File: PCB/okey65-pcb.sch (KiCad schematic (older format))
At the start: 14 parts

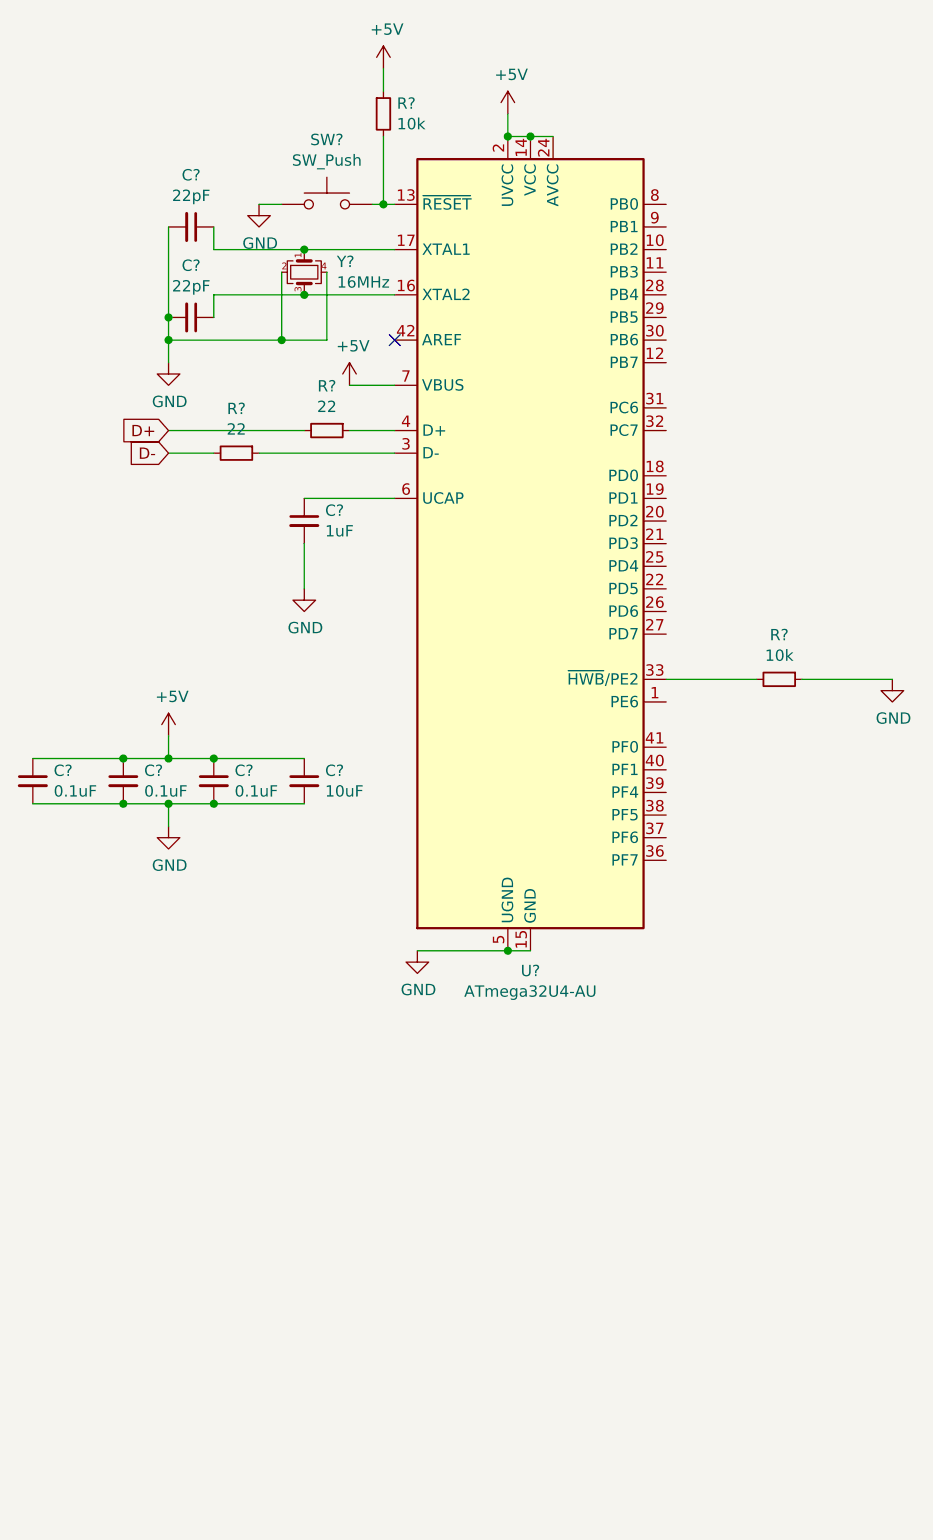
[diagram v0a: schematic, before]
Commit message: USB circuit shematic
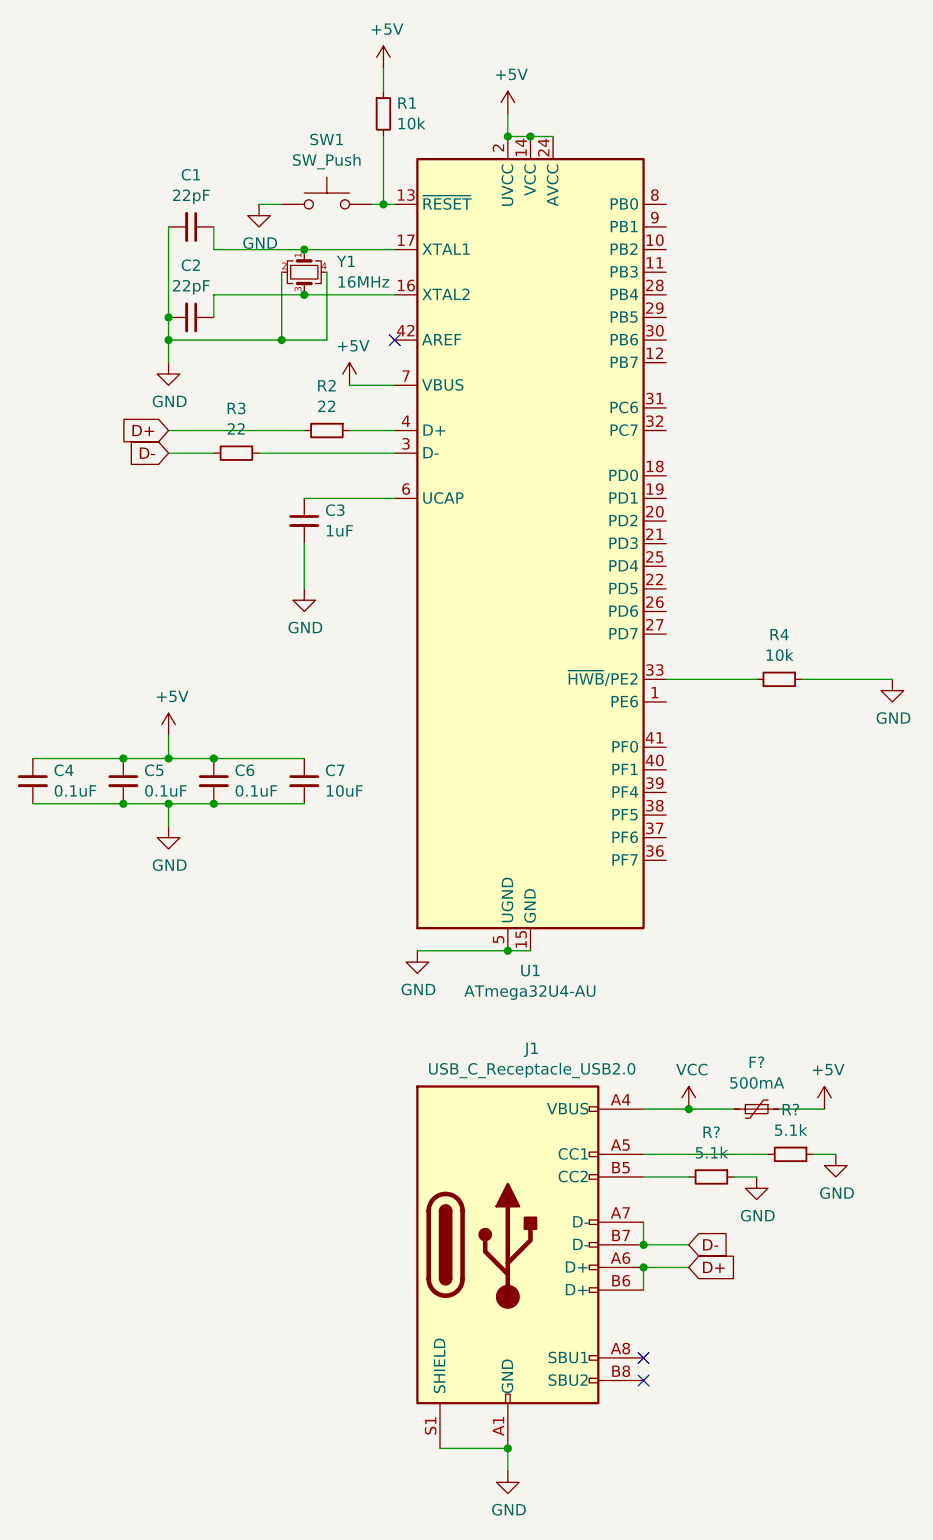
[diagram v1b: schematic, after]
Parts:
- added F?: 500mA, symbol Device:Polyfuse_Small
- added J1: USB_C_Receptacle_USB2.0, Connector_USB:USB_C_Receptacle_Palconn_UTC16-G, symbol Connector:USB_C_Receptacle_USB2.0
- added R? (x2): 5.1k, symbol Device:R_Small
- C1, C2, C3, C4, C5, C6, C7: renamed from C?; footprint (none) -> Capacitor_SMD:C_0805_2012Metric
- R1, R2, R3, R4: renamed from R?; footprint (none) -> Resistor_SMD:R_0805_2012Metric
- SW1: renamed from SW?; footprint (none) -> random-keyboard-parts:SKQG-1155865
- Y1: renamed from Y?; footprint (none) -> Crystal:Crystal_SMD_3225-4Pin_3.2x2.5mm
- gave numbers to parts that had none: 1
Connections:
- net +5V: now also F?.1
- net D+: now also J1.A6 (D+), J1.B6 (D+)
- net D-: now also J1.A7 (D-), J1.B7 (D-)
- net GND: now also J1.A1 (GND), J1.A12 (GND), J1.B1 (GND), J1.B12 (GND), J1.S1 (SHIELD), R?.1, R?.1
- new net: J1.A5 (CC1), R?.2
- new net: J1.B5 (CC2), R?.2
- new net VCC: F?.2, J1.A4 (VBUS), J1.A9 (VBUS), J1.B4 (VBUS), J1.B9 (VBUS)
- no-connect marks 1 -> 3

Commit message: Shema completed + pcb matrix
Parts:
- added D1, D10, D11, D12, D13, D14, D15, D16, D17, D18, D19, D2, D20, D21, D22, D23, D24, D25, D26, D27, D28, D29, D3, D30, D31, D32, D33, D34, D35, D36, D37, D38, D39, D4, D40, D41, D42, D43, D44, D45, D46, D47, D48, D49, D5, D50, D51, D52, D53, D54, D55, D56, D57, D58, D59, D6, D60, D61, D62, D63, D64, D65, D7, D8, D9: SOD-123, Diode_SMD:D_SOD-123, symbol Device:D_Small
- added D66, D67: LED, LED_SMD:LED_1206_3216Metric_ReverseMount_Hole1.8x2.4mm, symbol Device:LED
- added MX1, MX10, MX11, MX12, MX13, MX14, MX15, MX16, MX17, MX18, MX19, MX2, MX20, MX21, MX22, MX23, MX24, MX25, MX26, MX27, MX28, MX29, MX3, MX30, MX31, MX32, MX33, MX34, MX35, MX36, MX37, MX38, MX39, MX4, MX40, MX41, MX42, MX43, MX44, MX45, MX46, MX47, MX48, MX49, MX5, MX50, MX51, MX52, MX53, MX54, MX55, MX56, MX57, MX58, MX59, MX6, MX60, MX61, MX62, MX63, MX64, MX65, MX7, MX8, MX9: MX-NoLED, MX_Only:MXOnly-1U-NoLED, symbol MX_Alps_Hybrid:MX-NoLED
- added R5, R8: 80, Resistor_SMD:R_0805_2012Metric, symbol Device:R_Small
- F1: renamed from F?; footprint (none) -> Fuse:Fuse_1206_3216Metric
- R6, R7: renamed from R?; footprint (none) -> Resistor_SMD:R_0805_2012Metric
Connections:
- net GND: now also D66.1 (K), D67.1 (K)
- new net: D2.2 (A), MX2.2 (ROW)
- new net: D3.2 (A), MX3.2 (ROW)
- new net: D4.2 (A), MX4.2 (ROW)
- new net: D5.2 (A), MX5.2 (ROW)
- new net: D6.2 (A), MX6.2 (ROW)
- new net: D7.2 (A), MX7.2 (ROW)
- new net: D8.2 (A), MX8.2 (ROW)
- new net: D9.2 (A), MX9.2 (ROW)
- new net: D10.2 (A), MX10.2 (ROW)
- new net: D11.2 (A), MX11.2 (ROW)
- new net: D12.2 (A), MX12.2 (ROW)
- new net: D13.2 (A), MX13.2 (ROW)
- new net: D1.2 (A), MX1.2 (ROW)
- new net: D15.2 (A), MX15.2 (ROW)
- new net: D16.2 (A), MX16.2 (ROW)
- new net: D17.2 (A), MX17.2 (ROW)
- new net: D18.2 (A), MX18.2 (ROW)
- new net: D19.2 (A), MX19.2 (ROW)
- new net: D20.2 (A), MX20.2 (ROW)
- new net: D21.2 (A), MX21.2 (ROW)
- new net: D22.2 (A), MX22.2 (ROW)
- new net: D23.2 (A), MX23.2 (ROW)
- new net: D24.2 (A), MX24.2 (ROW)
- new net: D25.2 (A), MX25.2 (ROW)
- new net: D26.2 (A), MX26.2 (ROW)
- new net: D14.2 (A), MX14.2 (ROW)
- new net: D28.2 (A), MX28.2 (ROW)
- new net: D29.2 (A), MX29.2 (ROW)
- new net: D30.2 (A), MX30.2 (ROW)
- new net: D31.2 (A), MX31.2 (ROW)
- new net: D32.2 (A), MX32.2 (ROW)
- new net: D33.2 (A), MX33.2 (ROW)
- new net: D34.2 (A), MX34.2 (ROW)
- new net: D35.2 (A), MX35.2 (ROW)
- new net: D36.2 (A), MX36.2 (ROW)
- new net: D37.2 (A), MX37.2 (ROW)
- new net: D38.2 (A), MX38.2 (ROW)
- new net: D39.2 (A), MX39.2 (ROW)
- new net: D27.2 (A), MX27.2 (ROW)
- new net: D41.2 (A), MX41.2 (ROW)
- new net: D42.2 (A), MX42.2 (ROW)
- new net: D43.2 (A), MX43.2 (ROW)
- new net: D44.2 (A), MX44.2 (ROW)
- new net: D45.2 (A), MX45.2 (ROW)
- new net: D46.2 (A), MX46.2 (ROW)
- new net: D47.2 (A), MX47.2 (ROW)
- new net: D48.2 (A), MX48.2 (ROW)
- new net: D49.2 (A), MX49.2 (ROW)
- new net: D50.2 (A), MX50.2 (ROW)
- new net: D51.2 (A), MX51.2 (ROW)
- new net: D52.2 (A), MX52.2 (ROW)
- new net: D40.2 (A), MX40.2 (ROW)
- new net: D54.2 (A), MX54.2 (ROW)
- new net: D55.2 (A), MX55.2 (ROW)
- new net: D56.2 (A), MX56.2 (ROW)
- new net: D57.2 (A), MX57.2 (ROW)
- new net: D58.2 (A), MX58.2 (ROW)
- new net: D59.2 (A), MX59.2 (ROW)
- new net: D60.2 (A), MX60.2 (ROW)
- new net: D61.2 (A), MX61.2 (ROW)
- new net: D62.2 (A), MX62.2 (ROW)
- new net: D63.2 (A), MX63.2 (ROW)
- new net: D64.2 (A), MX64.2 (ROW)
- new net: D65.2 (A), MX65.2 (ROW)
- new net: D53.2 (A), MX53.2 (ROW)
- new net: D66.2 (A), R5.1
- new net: D67.2 (A), R8.1
- new net COL0: MX1.1 (COL), MX14.1 (COL), MX27.1 (COL), MX40.1 (COL), MX53.1 (COL)
- new net COL1: MX15.1 (COL), MX2.1 (COL), MX28.1 (COL), MX41.1 (COL), MX54.1 (COL)
- new net COL10: MX11.1 (COL), MX24.1 (COL), MX37.1 (COL), MX50.1 (COL), MX63.1 (COL)
- new net COL11: MX12.1 (COL), MX25.1 (COL), MX38.1 (COL), MX51.1 (COL), MX64.1 (COL)
- new net COL12: MX13.1 (COL), MX26.1 (COL), MX39.1 (COL), MX52.1 (COL), MX65.1 (COL)
- new net COL2: MX16.1 (COL), MX29.1 (COL), MX3.1 (COL), MX42.1 (COL), MX55.1 (COL)
- new net COL3: MX17.1 (COL), MX30.1 (COL), MX4.1 (COL), MX43.1 (COL), MX56.1 (COL)
- new net COL4: MX18.1 (COL), MX31.1 (COL), MX44.1 (COL), MX5.1 (COL), MX57.1 (COL)
- new net COL5: MX19.1 (COL), MX32.1 (COL), MX45.1 (COL), MX58.1 (COL), MX6.1 (COL)
- new net COL6: MX20.1 (COL), MX33.1 (COL), MX46.1 (COL), MX59.1 (COL), MX7.1 (COL)
- new net COL7: MX21.1 (COL), MX34.1 (COL), MX47.1 (COL), MX60.1 (COL), MX8.1 (COL)
- new net COL8: MX22.1 (COL), MX35.1 (COL), MX48.1 (COL), MX61.1 (COL), MX9.1 (COL)
- new net COL9: MX10.1 (COL), MX23.1 (COL), MX36.1 (COL), MX49.1 (COL), MX62.1 (COL)
- new net LED0: R5.2
- new net LED1: R8.2
- new net ROW0: D1.1 (K), D10.1 (K), D11.1 (K), D12.1 (K), D13.1 (K), D2.1 (K), D3.1 (K), D4.1 (K), D5.1 (K), D6.1 (K), D7.1 (K), D8.1 (K), D9.1 (K)
- new net ROW1: D14.1 (K), D15.1 (K), D16.1 (K), D17.1 (K), D18.1 (K), D19.1 (K), D20.1 (K), D21.1 (K), D22.1 (K), D23.1 (K), D24.1 (K), D25.1 (K), D26.1 (K)
- new net ROW2: D27.1 (K), D28.1 (K), D29.1 (K), D30.1 (K), D31.1 (K), D32.1 (K), D33.1 (K), D34.1 (K), D35.1 (K), D36.1 (K), D37.1 (K), D38.1 (K), D39.1 (K)
- new net ROW3: D40.1 (K), D41.1 (K), D42.1 (K), D43.1 (K), D44.1 (K), D45.1 (K), D46.1 (K), D47.1 (K), D48.1 (K), D49.1 (K), D50.1 (K), D51.1 (K), D52.1 (K)
- new net ROW4: D53.1 (K), D54.1 (K), D55.1 (K), D56.1 (K), D57.1 (K), D58.1 (K), D59.1 (K), D60.1 (K), D61.1 (K), D62.1 (K), D63.1 (K), D64.1 (K), D65.1 (K)
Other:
- moved on the sheet: C1, C2, C3, C4, C5, C6, C7, F1, J1, R1, R2, R3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

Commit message: Routing complete
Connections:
- net COL0: now also U1.41 (PF0)
- net COL1: now also U1.11 (PB3)
- net COL10: now also U1.31 (PC6)
- net COL11: now also U1.36 (PF7)
- net COL12: now also U1.37 (PF6)
- net COL2: now also U1.12 (PB7)
- net COL3: now also U1.22 (PD5)
- net COL4: now also U1.25 (PD4)
- net COL5: now also U1.26 (PD6)
- net COL6: now also U1.27 (PD7)
- net COL7: now also U1.28 (PB4)
- net COL8: now also U1.29 (PB5)
- net COL9: now also U1.30 (PB6)
- net LED0: now also U1.40 (PF1)
- net LED1: now also U1.32 (PC7)
- net ROW0: now also U1.20 (PD2)
- net ROW1: now also U1.21 (PD3)
- net ROW2: now also U1.1 (PE6)
- net ROW3: now also U1.39 (PF4)
- net ROW4: now also U1.38 (PF5)
- no-connect marks 3 -> 8
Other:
- moved on the sheet: F1
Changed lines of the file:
@@
 $EndDescr
-$Comp
-L MCU_Microchip_ATmega:ATmega32U4-AU U1
-U 1 1 61B8DF0D
-P 2750 3200
-F 0 "U1" H 2750 1311 50  0000 C CNN
-F 1 "ATmega32U4-AU" H 2750 1220 50  0000 C CNN
-F 2 "Package_QFP:TQFP-44_10x10mm_P0.8mm" H 2750 3200 50  0001 C CIN
-F 3 "http://ww1.microchip.com/downloads/en/DeviceDoc/Atmel-7766-8-bit-AVR-ATmega16U4-32U4_Datasheet.pdf" H 2750 3200 50  0001 C CNN
-	1    2750 3200
-	1    0    0    -1
-$EndComp
 $Comp
 L power:+5V #PWR02
 U 1 1 61B927E9
-P 2650 1300
-F 0 "#PWR02" H 2650 1150 50  0001 C CNN
-F 1 "+5V" H 2665 1473 50  0000 C CNN
-F 2 "" H 2650 1300 50  0001 C CNN
-F 3 "" H 2650 1300 50  0001 C CNN
-	1    2650 1300
-	1    0    0    -1
-$EndComp
-Wire Wire Line
-	2650 1300 2650 1400
-Wire Wire Line
-	2650 1400 2750 1400
-Connection ~ 2650 1400
-Wire Wire Line
-	2750 1400 2850 1400
-Connection ~ 2750 1400
-$Comp
-L power:GND #PWR010
-U 1 1 61B94874
-P 2250 5000
-F 0 "#PWR010" H 2250 4750 50  0001 C CNN
-F 1 "GND" H 2255 4827 50  0000 C CNN
-F 2 "" H 2250 5000 50  0001 C CNN
-F 3 "" H 2250 5000 50  0001 C CNN
-	1    2250 5000
-	1    0    0    -1
-$EndComp
-Wire Wire Line
-	2250 5000 2650 5000
-Wire Wire Line
-	2650 5000 2750 5000
-Connection ~ 2650 5000
+P 2650 1100
+F 0 "#PWR02" H 2650 950 50  0001 C CNN
+F 1 "+5V" H 2665 1273 50  0000 C CNN
+F 2 "" H 2650 1100 50  0001 C CNN
+F 3 "" H 2650 1100 50  0001 C CNN
+	1    2650 1100
+	1    0    0    -1
+$EndComp
 $Comp
 L Device:R_Small R4
@@
 Wire Wire Line
 	3350 3800 3500 3800
-Wire Wire Line
-	3700 3800 3850 3800
 $Comp
 L Device:R_Small R2
@@
 	1    0    0    -1
 $EndComp
-Wire Wire Line
-	1950 2500 2150 2500
 $Comp
 L Device:Crystal_GND24_Small Y1
@@
 L Device:Polyfuse_Small F1
 U 1 1 61C2DC78
-P 3750 5700
-F 0 "F1" V 3545 5700 50  0000 C CNN
-F 1 "500mA" V 3636 5700 50  0000 C CNN
-F 2 "Fuse:Fuse_1206_3216Metric" H 3800 5500 50  0001 L CNN
-F 3 "~" H 3750 5700 50  0001 C CNN
-	1    3750 5700
+P 4100 5700
+F 0 "F1" V 3895 5700 50  0000 C CNN
+F 1 "500mA" V 3986 5700 50  0000 C CNN
+F 2 "Fuse:Fuse_1206_3216Metric" H 4150 5500 50  0001 L CNN
+F 3 "~" H 4100 5700 50  0001 C CNN
+	1    4100 5700
 	0    1    1    0
 $EndComp
@@
 L power:+5V #PWR013
 U 1 1 61C30545
-P 4050 5700
-F 0 "#PWR013" H 4050 5550 50  0001 C CNN
-F 1 "+5V" H 4065 5873 50  0000 C CNN
-F 2 "" H 4050 5700 50  0001 C CNN
-F 3 "" H 4050 5700 50  0001 C CNN
-	1    4050 5700
+P 4400 5700
+F 0 "#PWR013" H 4400 5550 50  0001 C CNN
+F 1 "+5V" H 4415 5873 50  0000 C CNN
+F 2 "" H 4400 5700 50  0001 C CNN
+F 3 "" H 4400 5700 50  0001 C CNN
+	1    4400 5700
 	1    0    0    -1
 $EndComp
@@
 L power:VCC #PWR012
 U 1 1 61C311D5
-P 3450 5700
-F 0 "#PWR012" H 3450 5550 50  0001 C CNN
-F 1 "VCC" H 3465 5873 50  0000 C CNN
-F 2 "" H 3450 5700 50  0001 C CNN
-F 3 "" H 3450 5700 50  0001 C CNN
-	1    3450 5700
-	1    0    0    -1
-$EndComp
-Wire Wire Line
-	3250 5700 3450 5700
-Wire Wire Line
-	3450 5700 3650 5700
-Connection ~ 3450 5700
-Wire Wire Line
-	3850 5700 4050 5700
+P 3800 5700
+F 0 "#PWR012" H 3800 5550 50  0001 C CNN
+F 1 "VCC" H 3815 5873 50  0000 C CNN
+F 2 "" H 3800 5700 50  0001 C CNN
+F 3 "" H 3800 5700 50  0001 C CNN
+	1    3800 5700
+	1    0    0    -1
+$EndComp
+Wire Wire Line
+	3800 5700 4000 5700
+Connection ~ 3800 5700
+Wire Wire Line
+	4200 5700 4400 5700
 Text GLabel 3450 6400 2    50   Input ~ 0
 D+
@@
 	0    -1   -1   0
 $EndComp
-Wire Wire Line
-	4500 3300 4600 3300
 Text GLabel 4300 3500 0    50   Input ~ 0
 ROW2
@@
 Wire Wire Line
 	8550 6000 8950 6000
+Text GLabel 3450 4200 2    50   Input ~ 0
+LED0
+Wire Wire Line
+	3450 3900 3350 3900
+Text GLabel 3450 2000 2    50   Input ~ 0
+COL1
+Wire Wire Line
+	3450 2000 3350 2000
+Text GLabel 3450 4400 2    50   Input ~ 0
+ROW4
+Wire Wire Line
+	3450 4400 3350 4400
+Text GLabel 3450 3900 2    50   Input ~ 0
+ROW2
+Text GLabel 3450 2400 2    50   Input ~ 0
+COL2
+Wire Wire Line
+	3450 2400 3350 2400
+Text GLabel 3450 3400 2    50   Input ~ 0
+COL3
+Wire Wire Line
+	3450 3400 3350 3400
+Text GLabel 3450 3200 2    50   Input ~ 0
+ROW1
+Wire Wire Line
+	3450 3200 3350 3200
+Wire Wire Line
+	3450 4100 3350 4100
+Text GLabel 3450 4100 2    50   Input ~ 0
+COL0
+Text GLabel 3450 3100 2    50   Input ~ 0
+ROW0
+Wire Wire Line
+	3450 3100 3350 3100
+Wire Wire Line
+	3450 4200 3350 4200
+Text GLabel 3450 2700 2    50   Input ~ 0
+LED1
+Wire Wire Line
+	3450 2700 3350 2700
+Text GLabel 3450 4300 2    50   Input ~ 0
+ROW3
+Wire Wire Line
+	3450 4300 3350 4300
+Text GLabel 3450 3300 2    50   Input ~ 0
+COL4
+Wire Wire Line
+	3450 3300 3350 3300
+Text GLabel 3450 3500 2    50   Input ~ 0
+COL5
+Text GLabel 3450 3600 2    50   Input ~ 0
+COL6
+Text GLabel 3450 2100 2    50   Input ~ 0
+COL7
+Text GLabel 3450 2200 2    50   Input ~ 0
+COL8
+Text GLabel 3450 2300 2    50   Input ~ 0
+COL9
+Text GLabel 3450 2600 2    50   Input ~ 0
+COL10
+Wire Wire Line
+	3350 2100 3450 2100
+Wire Wire Line
+	3350 2200 3450 2200
+Wire Wire Line
+	3350 2300 3450 2300
+Wire Wire Line
+	3350 2600 3450 2600
+Wire Wire Line
+	3350 3500 3450 3500
+Wire Wire Line
+	3350 3600 3450 3600
+Text GLabel 3450 4500 2    50   Input ~ 0
+COL12
+Wire Wire Line
+	3350 4500 3450 4500
+Text GLabel 3450 4600 2    50   Input ~ 0
+COL11
+Wire Wire Line
+	3350 4600 3450 4600
+NoConn ~ 3350 1700
+NoConn ~ 3350 1800
+NoConn ~ 3350 1900
+NoConn ~ 3350 2900
+NoConn ~ 3350 3000
+$Comp
+L power:PWR_FLAG #FLG0101
+U 1 1 621C59A9
+P 3500 5700
+F 0 "#FLG0101" H 3500 5775 50  0001 C CNN
+F 1 "PWR_FLAG" H 3500 5873 50  0000 C CNN
+F 2 "" H 3500 5700 50  0001 C CNN
+F 3 "~" H 3500 5700 50  0001 C CNN
+	1    3500 5700
+	1    0    0    -1
+$EndComp
+$Comp
+L power:PWR_FLAG #FLG0102
+U 1 1 621DEA4F
+P 2650 1250
+F 0 "#FLG0102" H 2650 1325 50  0001 C CNN
+F 1 "PWR_FLAG" V 2650 1378 50  0000 L CNN
+F 2 "" H 2650 1250 50  0001 C CNN
+F 3 "~" H 2650 1250 50  0001 C CNN
+	1    2650 1250
+	0    1    1    0
+$EndComp
+Wire Wire Line
+	1950 2500 2150 2500
+$Comp
+L power:GND #PWR010
+U 1 1 61B94874
+P 2250 5100
+F 0 "#PWR010" H 2250 4850 50  0001 C CNN
+F 1 "GND" H 2255 4927 50  0000 C CNN
+F 2 "" H 2250 5100 50  0001 C CNN
+F 3 "" H 2250 5100 50  0001 C CNN
+	1    2250 5100
+	1    0    0    -1
+$EndComp
+Wire Wire Line
+	2250 5000 2250 5100
+$Comp
+L power:PWR_FLAG #FLG0103
+U 1 1 6226213E
+P 2250 5000
+F 0 "#FLG0103" H 2250 5075 50  0001 C CNN
+F 1 "PWR_FLAG" V 2250 5127 50  0000 L CNN
+F 2 "" H 2250 5000 50  0001 C CNN
+F 3 "~" H 2250 5000 50  0001 C CNN
+	1    2250 5000
+	0    -1   -1   0
+$EndComp
+Connection ~ 2250 5000
+Connection ~ 2650 5000
+Connection ~ 2750 1400
+Wire Wire Line
+	2750 1400 2850 1400
+Wire Wire Line
+	2650 1400 2750 1400
+Wire Wire Line
+	2650 5000 2250 5000
+Wire Wire Line
+	2650 5000 2750 5000
+Wire Wire Line
+	3700 3800 3850 3800
+Wire Wire Line
+	4500 3300 4600 3300
+$Comp
+L MCU_Microchip_ATmega:ATmega32U4-AU U1
+U 1 1 61B8DF0D
+P 2750 3200
+F 0 "U1" H 2750 1311 50  0000 C CNN
+F 1 "ATmega32U4-AU" H 2750 1220 50  0000 C CNN
+F 2 "Package_QFP:TQFP-44_10x10mm_P0.8mm" H 2750 3200 50  0001 C CIN
+F 3 "http://ww1.microchip.com/downloads/en/DeviceDoc/Atmel-7766-8-bit-AVR-ATmega16U4-32U4_Datasheet.pdf" H 2750 3200 50  0001 C CNN
+	1    2750 3200
+	1    0    0    -1
+$EndComp
+Wire Wire Line
+	3500 5700 3800 5700
+Wire Wire Line
+	3250 5700 3500 5700
+Connection ~ 3500 5700
+Wire Wire Line
+	2650 1100 2650 1250
+Wire Wire Line
+	2650 1250 2650 1400
+Connection ~ 2650 1250
+Connection ~ 2650 1400
 $EndSCHEMATC

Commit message: Hardware almost complete
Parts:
- C1, C2: LCSC (none) -> C1804
- C3: LCSC (none) -> C116352
- C4, C5, C6: LCSC (none) -> C286511
- C7: LCSC (none) -> C77075
- D1, D10, D11, D12, D13, D14, D15, D16, D17, D18, D19, D2, D20, D21, D22, D23, D24, D25, D26, D27, D28, D29, D3, D30, D31, D32, D33, D34, D35, D36, D37, D38, D39, D4, D40, D41, D42, D43, D44, D45, D46, D47, D48, D49, D5, D50, D51, D52, D53, D54, D55, D56, D57, D58, D59, D6, D60, D61, D62, D63, D64, D65, D7, D8, D9: LCSC (none) -> C81598
- D66, D67: LCSC (none) -> C401114
- F1: LCSC (none) -> C883125
- J1: LCSC (none) -> C136423
- R1, R4: LCSC (none) -> C406725
- R2, R3: LCSC (none) -> C25295
- R5, R8: value 80 -> 68; LCSC (none) -> C17802
- R6, R7: LCSC (none) -> C27834
- SW1: LCSC (none) -> C221929
- U1: LCSC (none) -> C44854
- Y1: LCSC (none) -> C213410
